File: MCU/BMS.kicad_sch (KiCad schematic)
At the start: 35 parts, among them J301 Battery, J302 Battery, Q301 2SB1198K, Q302 2SB1198K, Q303 2N7002, Q304 2SB1198K, Q305 2N7002, Q306 2SC2412K, Q307 PJA3404A, Q308 PJA3404A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

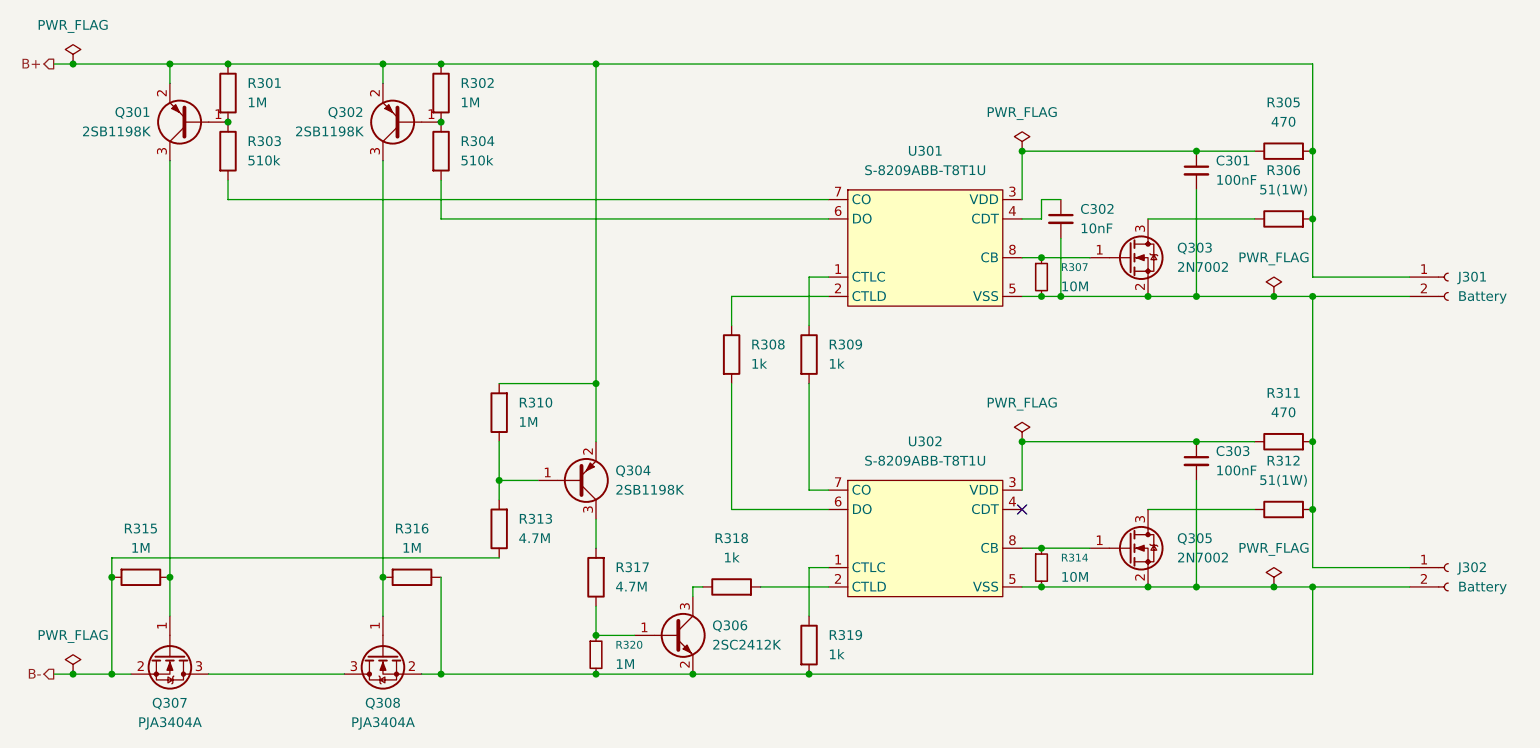
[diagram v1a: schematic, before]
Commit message: Update: コネクタをだいぶ消した
手配線になるね
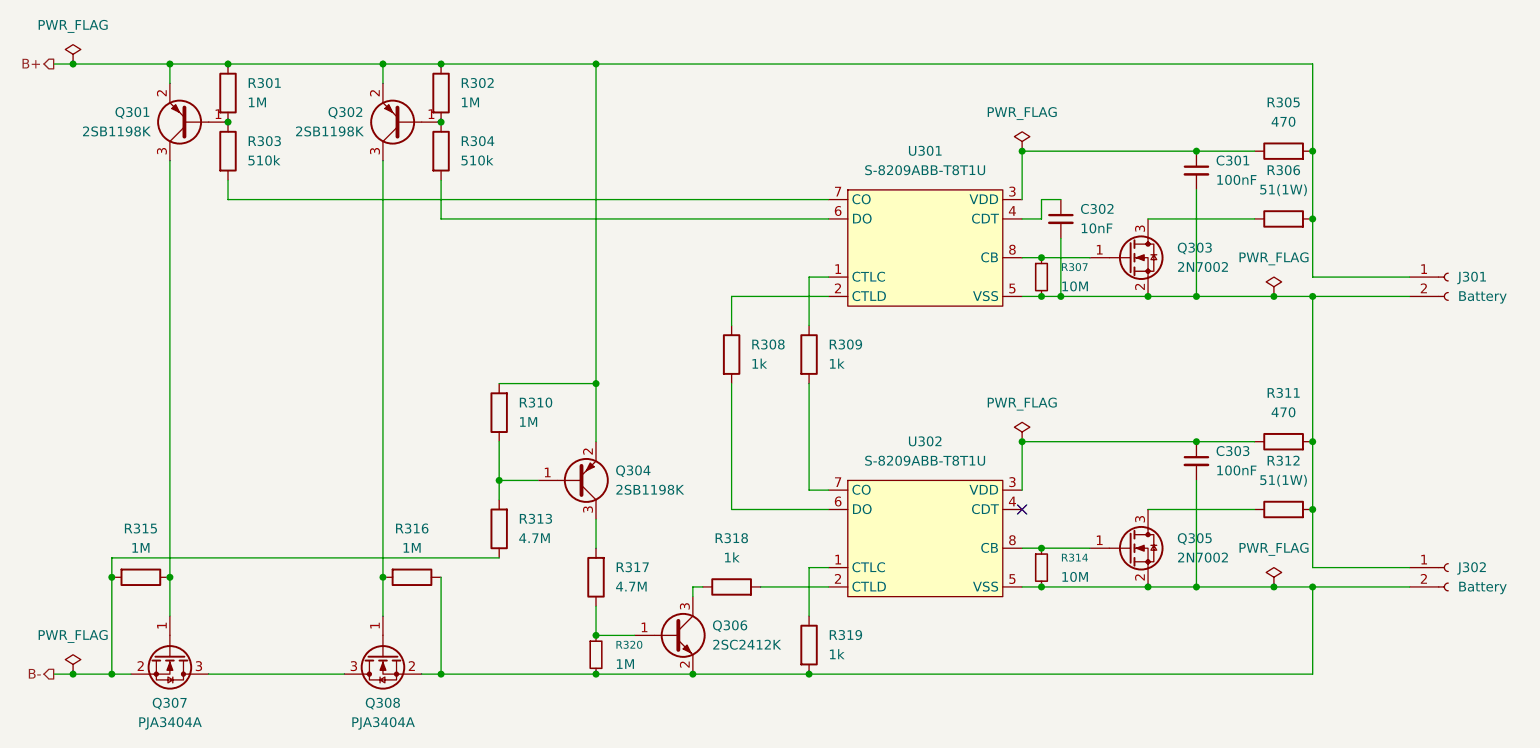
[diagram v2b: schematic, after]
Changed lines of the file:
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@@
 			)
 		)
-		(property "Datasheet" "https://www.mouser.jp/datasheet/2/1057/PJA3404A-1867251.pdf"
+		(property "Datasheet" "http://www.diodes.com/assets/Datasheets/DMG3404L.pdf"
 			(at 106.68 140.97 0)
 			(hide yes)
@@
 			)
 		)
-		(property "Description" "5.6A Id, 30V Vds, N-Channel MOSFET, SOT-23"
+		(property "Description" "5.8A Id, 30V Vds, N-Channel MOSFET, SOT-23"
 			(at 106.68 140.97 0)
 			(hide yes)
@@
 	)
 	(symbol
+		(lib_name "DMG3404L_1")
 		(lib_id "Transistor_FET:DMG3404L")
 		(at 78.74 140.97 270)
@@
 			)
 		)
-		(property "Datasheet" "https://www.mouser.jp/datasheet/2/1057/PJA3404A-1867251.pdf"
+		(property "Datasheet" "http://www.diodes.com/assets/Datasheets/DMG3404L.pdf"
 			(at 78.74 140.97 0)
 			(hide yes)
@@
 			)
 		)
-		(property "Description" "5.6A Id, 30V Vds, N-Channel MOSFET, SOT-23"
+		(property "Description" "5.8A Id, 30V Vds, N-Channel MOSFET, SOT-23"
 			(at 78.74 140.97 0)
 			(hide yes)
@@
 	)
 	(symbol
+		(lib_name "2N7002_1")
 		(lib_id "Transistor_FET:2N7002")
 		(at 204.47 127 0)
